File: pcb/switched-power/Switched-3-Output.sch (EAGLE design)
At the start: 39 parts, among them SW1 SPDT-100SP4, SW2 SPDT-100SP4, SW3 SPDT-100SP4

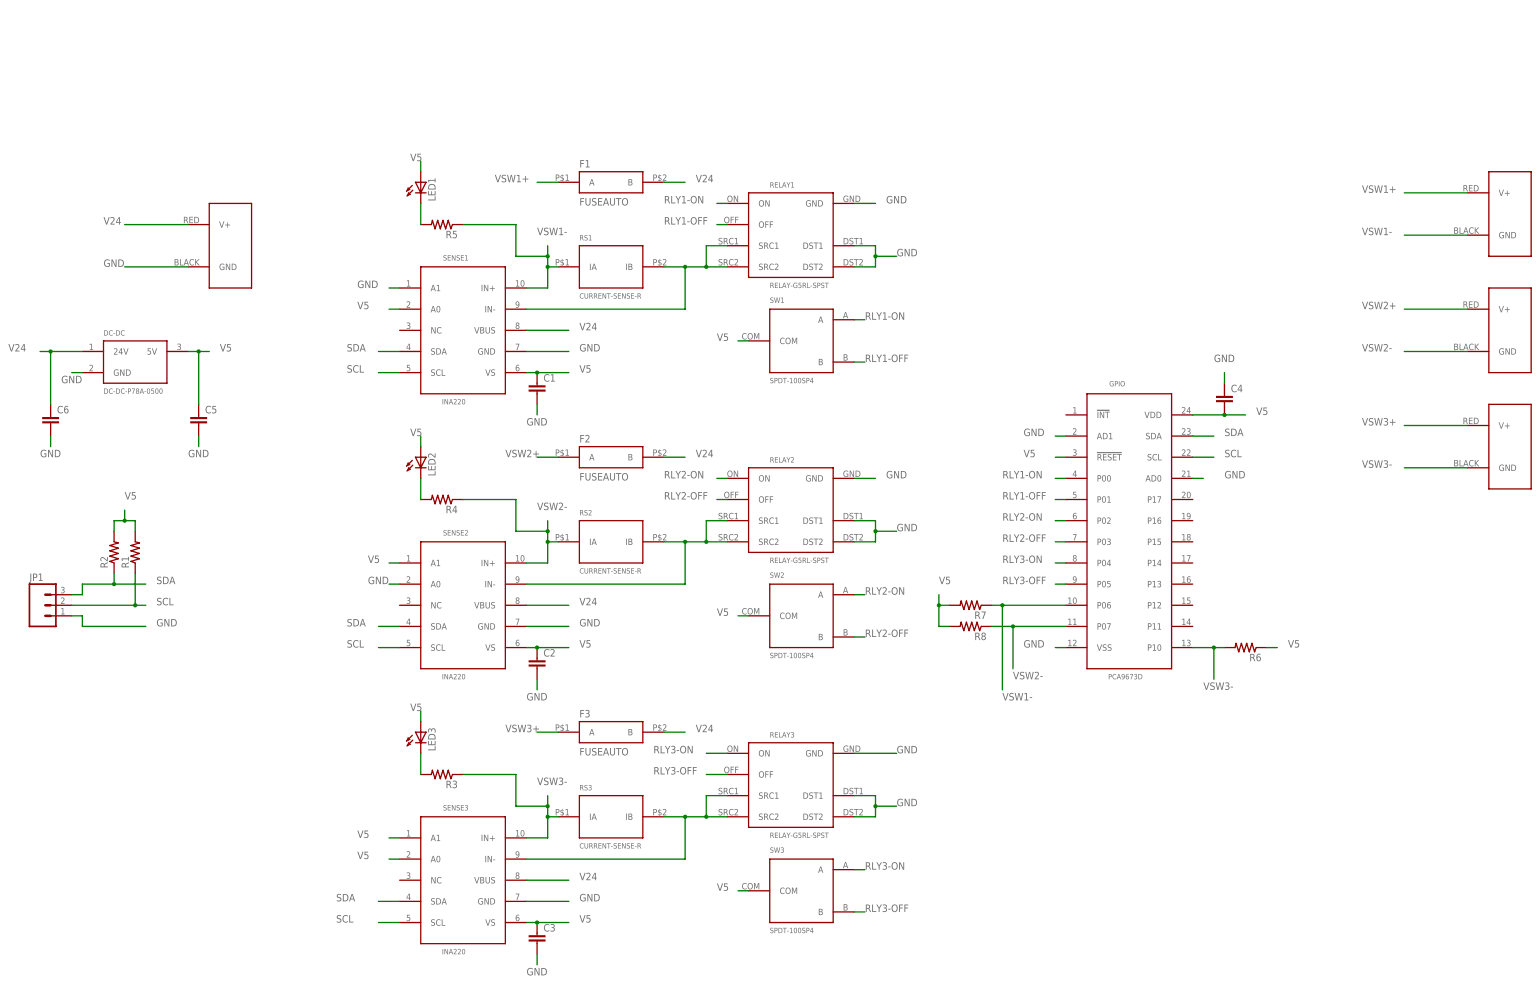
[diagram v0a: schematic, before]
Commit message: Add gitignore, plus make new revision with latest board
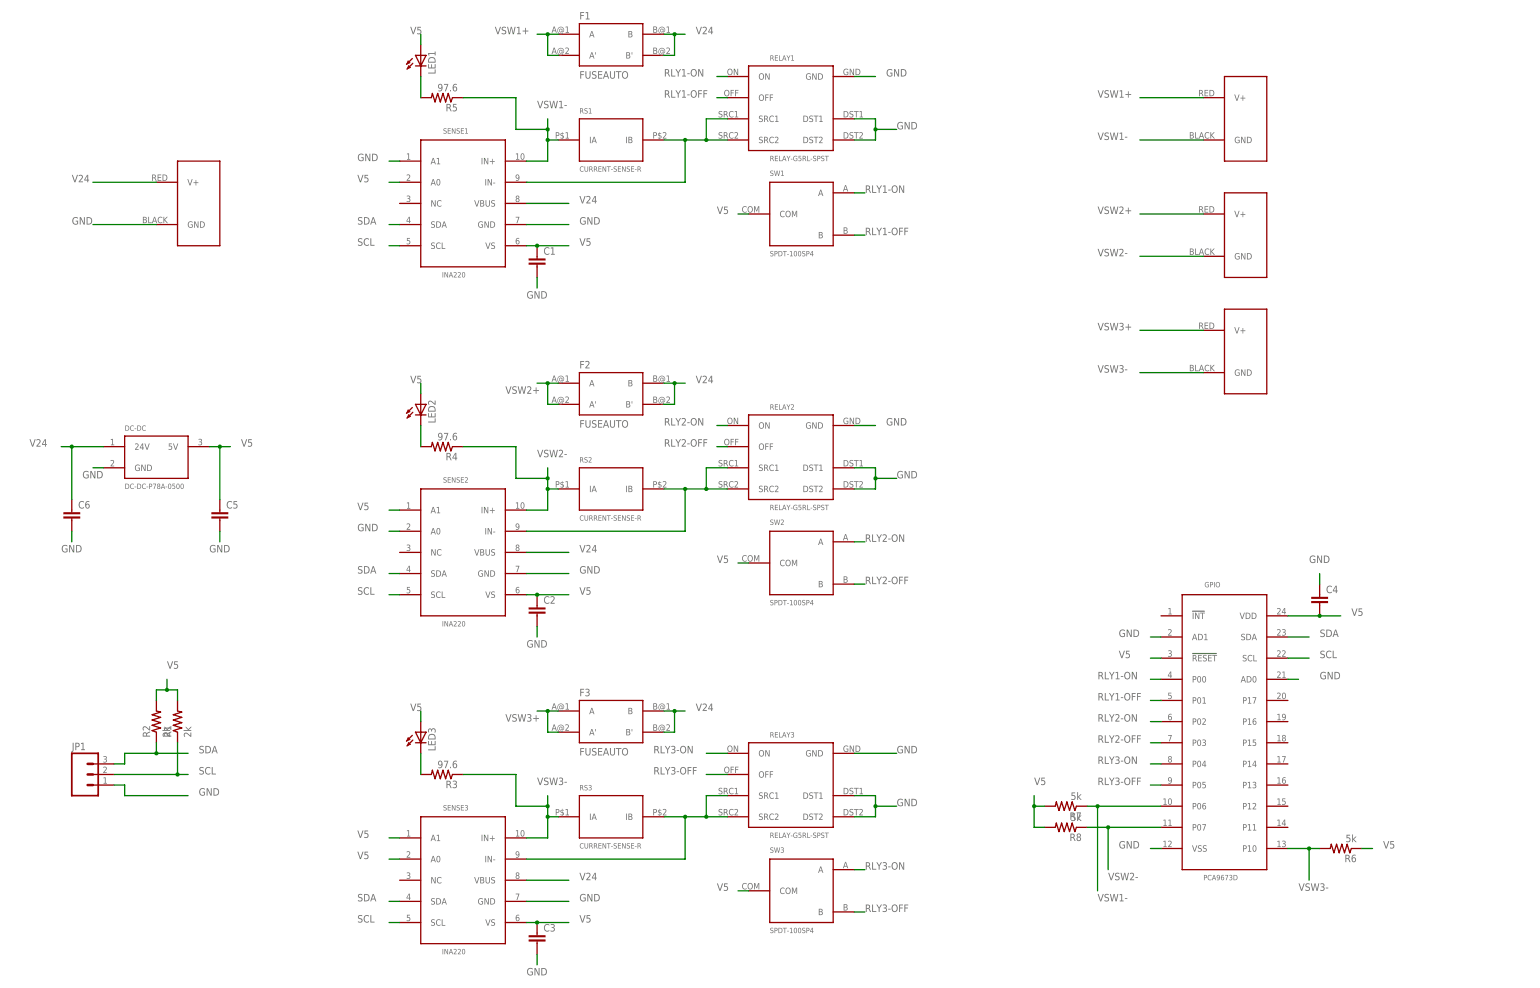
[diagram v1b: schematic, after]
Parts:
- R1, R2: value (none) -> 2k
- R3, R4, R5: value (none) -> 97.6
- R6, R7, R8: value (none) -> 5k
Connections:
- net V24: now also F1.B', F2.B', F3.B'
- net VSW1+: now also F1.A'
- net VSW2+: now also F2.A'
- net VSW3+: now also F3.A'
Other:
- moved on the sheet: C1, C2, C4, C5, C6, DC-DC, GPIO, JP1, LED1, LED2, R1, R2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
